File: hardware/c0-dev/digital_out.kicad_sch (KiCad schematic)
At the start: 51 parts, among them Q10 BSS138P, Q3 BSS138P, Q4 BSS138P, Q5 BSS138P, Q6 BSS138P, Q7 BSS138P, Q8 BSS138P, Q9 BSS138P, U35 B0505S-1WR3, U36 ISO1540, U37 TLP175A, U38 TCA9555PWR, U39 TPS4H000A-Q1, U40 TPS4H000A-Q1

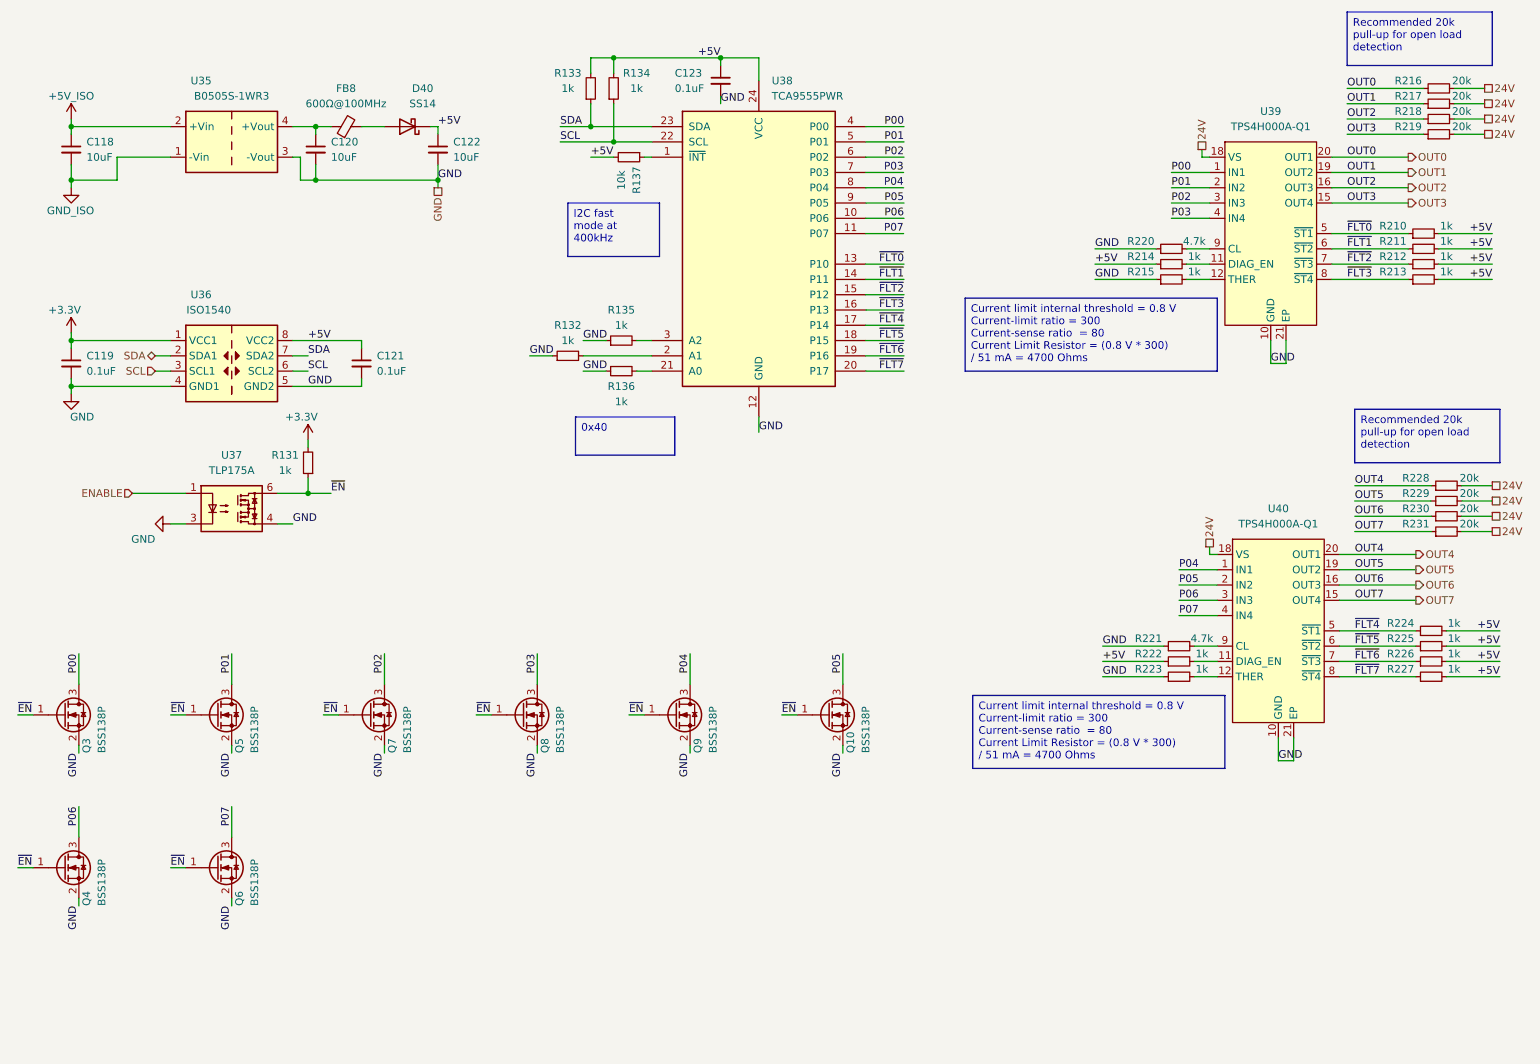
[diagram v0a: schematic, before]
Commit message: page based annotation + flybuck fb
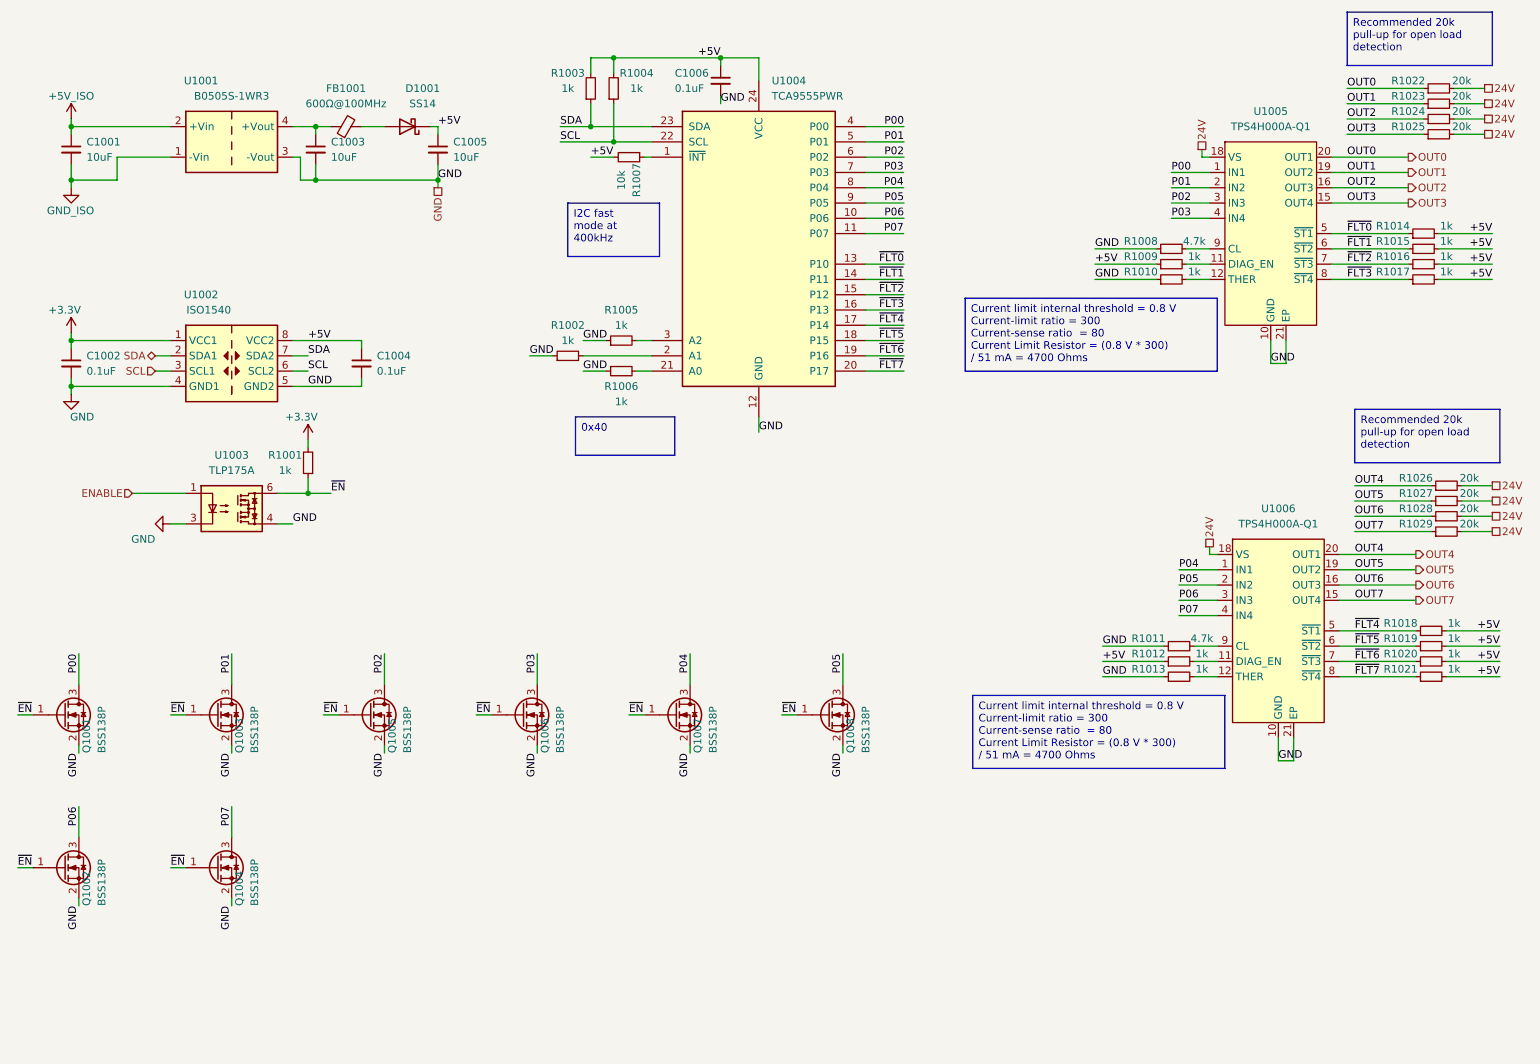
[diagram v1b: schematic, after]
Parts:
- renumbered C118 to C1001, C119 to C1002, C120 to C1003, C121 to C1004, C122 to C1005, C123 to C1006, D40 to D1001, FB8 to FB1001, Q3 to Q1001, Q4 to Q1002, Q5 to Q1003, Q6 to Q1004, Q7 to Q1005, Q8 to Q1006, Q9 to Q1007, Q10 to Q1008, R131 to R1001, R132 to R1002, R133 to R1003, R134 to R1004, R135 to R1005, R136 to R1006, R137 to R1007, R220 to R1008, R214 to R1009, R215 to R1010, R221 to R1011, R222 to R1012, R223 to R1013, R210 to R1014, R211 to R1015, R212 to R1016, R213 to R1017, R224 to R1018, R225 to R1019, R226 to R1020, R227 to R1021, R216 to R1022, R217 to R1023, R218 to R1024, R219 to R1025, R228 to R1026, R229 to R1027, R230 to R1028, R231 to R1029, U35 to U1001, U36 to U1002, U37 to U1003, U38 to U1004, U39 to U1005, U40 to U1006

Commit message: power and isolation cleanup
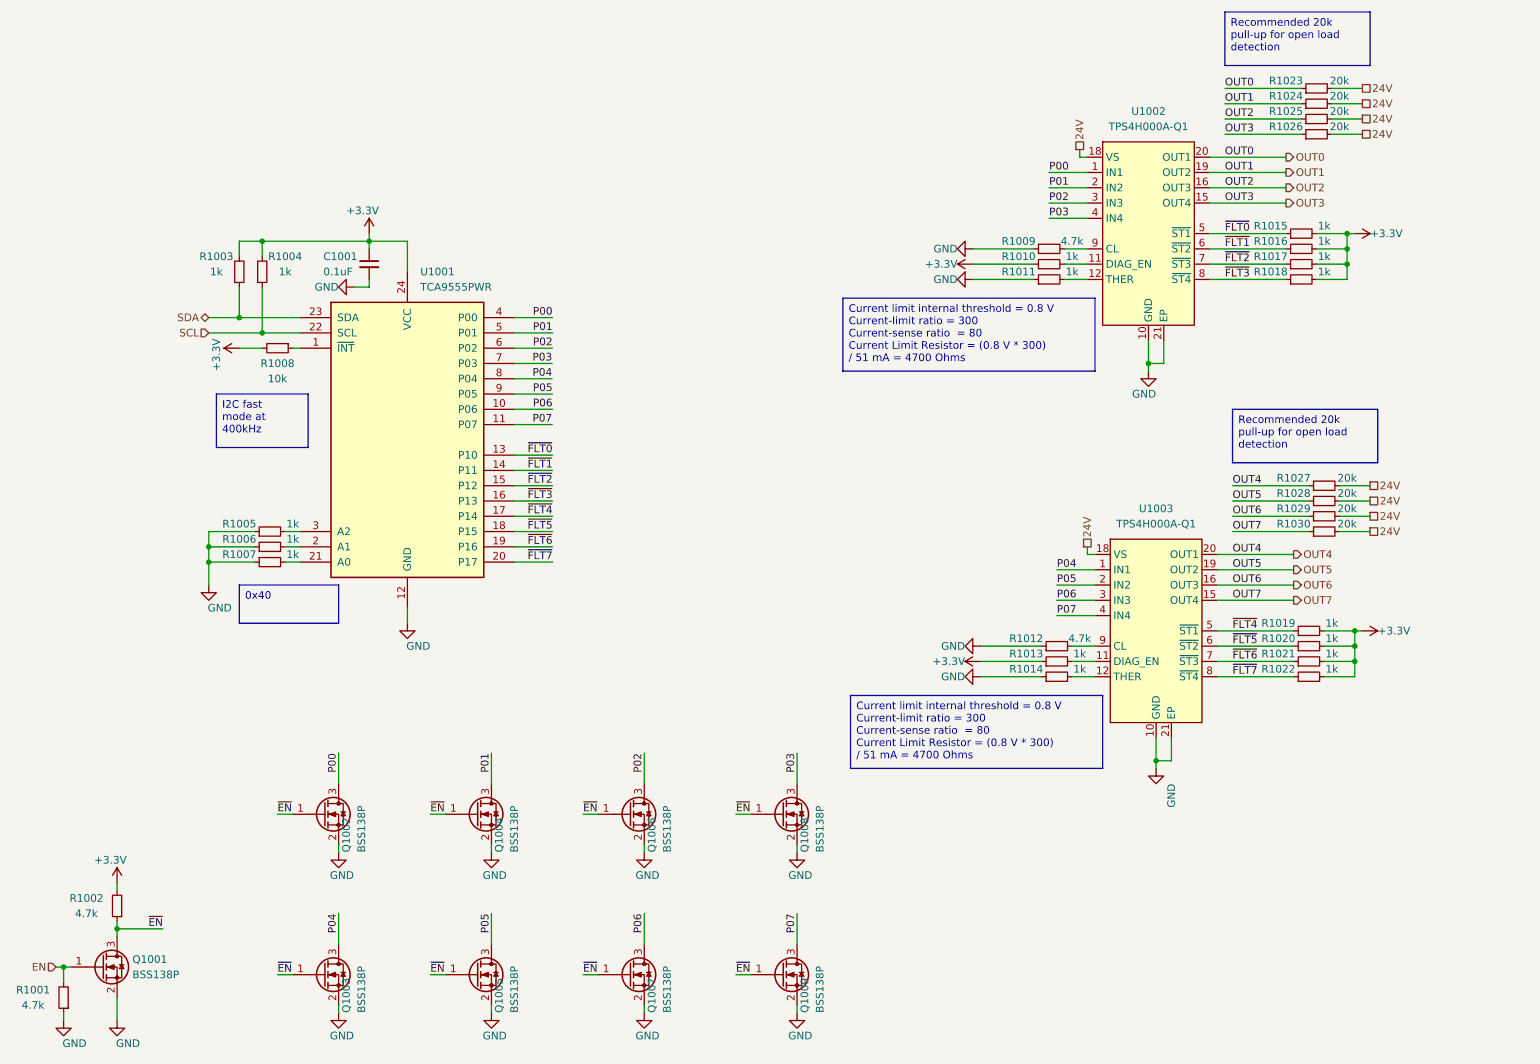
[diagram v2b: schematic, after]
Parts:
- removed C1001, C1003, C1005: 10uF, Capacitor_SMD:C_0805_2012Metric, symbol Device:C_Small
- removed C1002, C1004: 0.1uF, Capacitor_SMD:C_0402_1005Metric, symbol Device:C_Small
- removed D1001: SS14, Diode_SMD:D_SMA, symbol Diode:B140-E3
- removed FB1001: 600Ω@100MHz, Inductor_SMD:L_0603_1608Metric, symbol Device:FerriteBead_Small
- removed U1001: B0505S-1WR3, Converter_DCDC:Converter_DCDC_Murata_MEE1SxxxxSC_THT, symbol Converter_DCDC:MEE1S0505SC
- removed U1002: ISO1540, Package_SO:SOIC-8_3.9x4.9mm_P1.27mm, symbol Isolator:ISO1540
- removed U1003: TLP175A, Package_SO:Toshiba_SOIC-4-6_4.4x3.6mm_P1.27mm, symbol Relay_SolidState:TLP175A
- added Q1001: BSS138P, Package_TO_SOT_SMD:SOT-23, symbol Transistor_FET:Q_NMOS_GSD
- added R1002: 4.7k, Resistor_SMD:R_0402_1005Metric, symbol Device:R_Small
- R1001: value 1k -> 4.7k
- renumbered C1006 to C1001, Q1001 to Q1002, Q1007 to Q1003, Q1003 to Q1004, Q1008 to Q1005, Q1005 to Q1006, Q1002 to Q1007, Q1006 to Q1008, Q1004 to Q1009, R1002 to R1006, R1006 to R1007, R1007 to R1008, R1008 to R1009, R1009 to R1010, R1010 to R1011, R1011 to R1012, R1012 to R1013, R1013 to R1014, R1014 to R1015, R1015 to R1016, R1016 to R1017, R1017 to R1018, R1018 to R1019, R1019 to R1020, R1020 to R1021, R1021 to R1022, R1022 to R1023, R1023 to R1024, R1024 to R1025, R1025 to R1026, R1026 to R1027, R1027 to R1028, R1028 to R1029, R1029 to R1030, U1004 to U1001, U1005 to U1002, U1006 to U1003
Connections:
- net +5V is gone; now on net +3.3V: C1001.1, R1003.2, R1004.2, R1008.2, R1010.1, R1013.1, R1015.2, R1016.2, R1017.2, R1018.2, R1019.2, R1020.2, R1021.2, R1022.2, U1001.24 (VCC)
- net +3.3V: now also R1002.2; no longer R1001.2
- net GND: now also R1001.1, Q1001.2 (S)
- net ~{EN}: now also Q1001.3 (D), R1002.1; no longer R1001.1
- new net EN: Q1001.1 (G), R1001.2
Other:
- moved on the sheet: C1001, Q1002, Q1003, Q1004, Q1005, Q1006, Q1007, Q1008, Q1009, R1003, R1004, R1005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

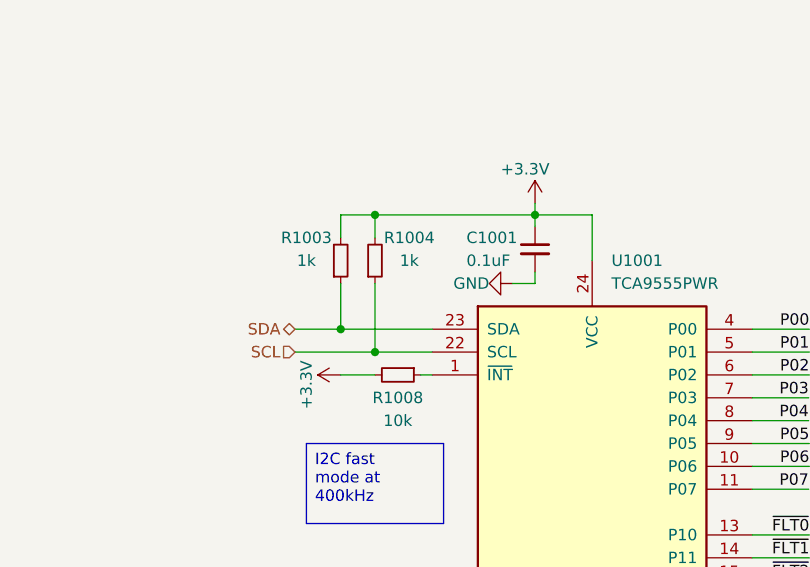
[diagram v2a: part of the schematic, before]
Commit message: inital placement done
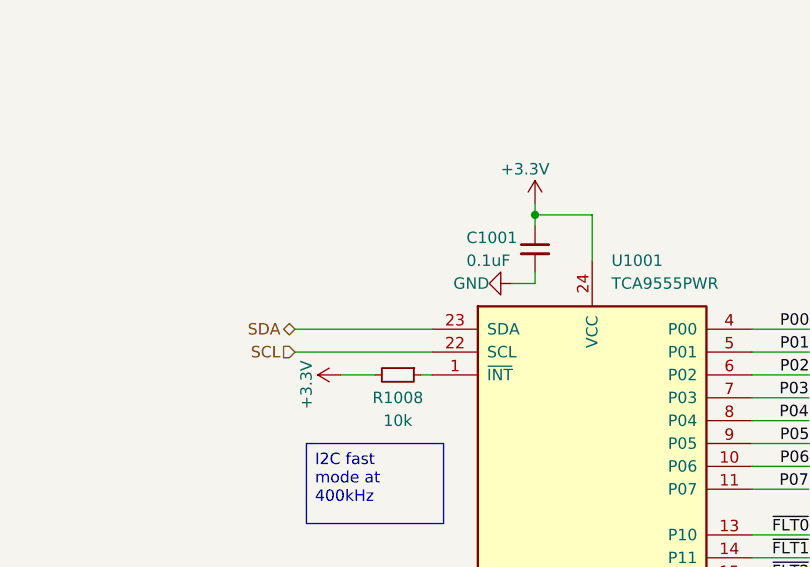
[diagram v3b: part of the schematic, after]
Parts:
- removed R1003, R1004: 1k, Resistor_SMD:R_0402_1005Metric, symbol Device:R_Small
